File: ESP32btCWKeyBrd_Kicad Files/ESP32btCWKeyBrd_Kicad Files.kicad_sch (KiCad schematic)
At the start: 20 parts, among them J1 CW Key Out, J2 3.5" TFT ILI9488, J3 Audio In Jack, J4 Conn_01x02_MountingPin, Q1 MMBT3904, Q2 MMBT3906, Q3 D4184, U1 ESP32-DEVKIT-V1

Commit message: Incremental Commit
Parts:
- added SW1: SW_Push_SPDT, symbol Switch:SW_Push_SPDT
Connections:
- net +5V: now also SW1.3 (C); no longer J4.1 (Pin_1)
- new net: J4.1 (Pin_1), SW1.2 (B)
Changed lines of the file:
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@@
+    (stroke (width 0) (type default))
+  )
+  (wire (pts (xy 130.81 38.1) (xy 140.97 38.1))
     (stroke (width 0) (type default))
   )
@@
         (path "/3f3f0b47-94ce-4e4b-9adc-e767077ae590"
           (reference "Q2") (unit 1)
+        )
+      )
+    )
+  )
+  (symbol (lib_id "Switch:SW_Push_SPDT") (at 125.73 38.1 0) (mirror y) (unit 1)
+    (in_bom yes) (on_board yes) (dnp no) (fields_autoplaced)
+    (property "Reference" "SW1" (at 125.73 30.48 0)
+      (effects (font (size 1.27 1.27)))
+    )
+    (property "Value" "SW_Push_SPDT" (at 125.73 33.02 0)
+      (effects (font (size 1.27 1.27)))
+    )
+    (property "Footprint" "" (at 125.73 38.1 0)
+      (effects (font (size 1.27 1.27)) hide)
+    )
+    (property "Datasheet" "~" (at 125.73 38.1 0)
+      (effects (font (size 1.27 1.27)) hide)
+    )
+    (pin "3")
+    (pin "1")
+    (pin "2")
+    (instances
+      (project "ESP32btCWKeyBrd_Kicad Files"
+        (path "/3f3f0b47-94ce-4e4b-9adc-e767077ae590"
+          (reference "SW1") (unit 1)
         )
       )
@@
     )
   )
-  (symbol (lib_id "power:+5V") (at 140.97 38.1 90) (unit 1)
-    (in_bom yes) (on_board yes) (dnp no) (fields_autoplaced)
-    (property "Reference" "#PWR015" (at 144.78 38.1 0)
-      (effects (font (size 1.27 1.27)) hide)
-    )
-    (property "Value" "+5V" (at 137.16 38.1 90)
-      (effects (font (size 1.27 1.27)) (justify left))
-    )
-    (property "Footprint" "" (at 140.97 38.1 0)
-      (effects (font (size 1.27 1.27)) hide)
-    )
-    (property "Datasheet" "" (at 140.97 38.1 0)
-      (effects (font (size 1.27 1.27)) hide)
-    )
+  (symbol (lib_id "power:+5V") (at 120.65 40.64 90) (unit 1)
+    (in_bom yes) (on_board yes) (dnp no) (fields_autoplaced)
+    (property "Reference" "#PWR015" (at 124.46 40.64 0)
+      (effects (font (size 1.27 1.27)) hide)
+    )
+    (property "Value" "+5V" (at 116.84 40.64 90)
+      (effects (font (size 1.27 1.27)) (justify left))
+    )
+    (property "Footprint" "" (at 120.65 40.64 0)
+      (effects (font (size 1.27 1.27)) hide)
+    )
+    (property "Datasheet" "" (at 120.65 40.64 0)
+      (effects (font (size 1.27 1.27)) hide)
+    )

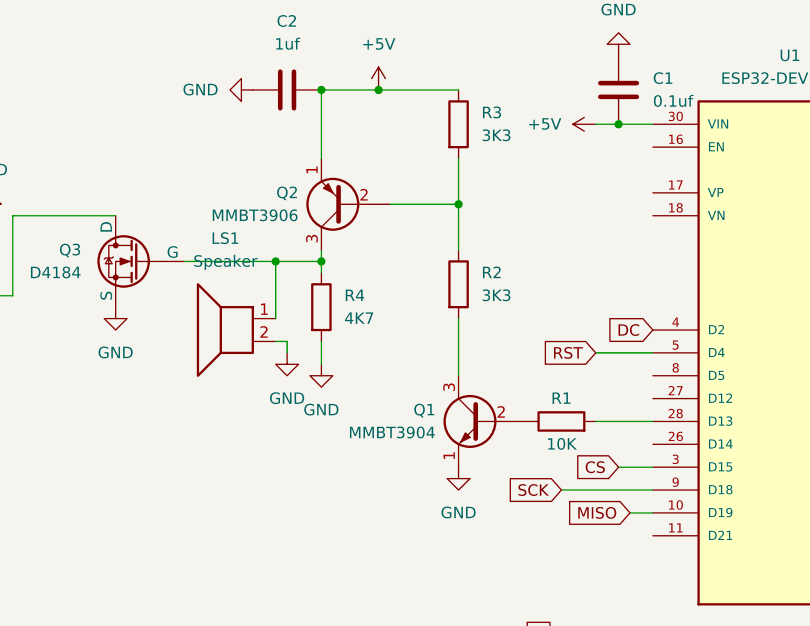
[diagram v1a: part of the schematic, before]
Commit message: Fixed the PCB
Unfortunately after I ordered the original set :(
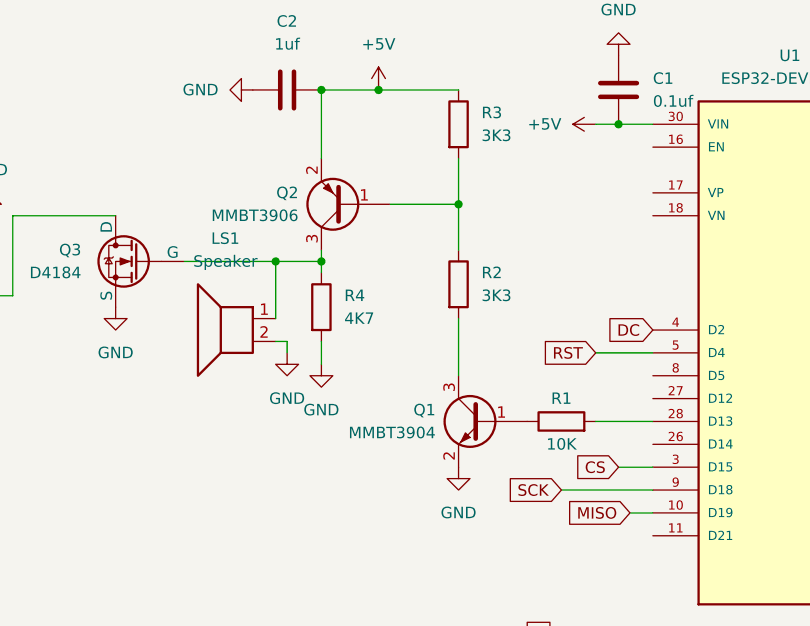
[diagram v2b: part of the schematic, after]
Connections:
- net +5V: now also Q2.2 (E); no longer Q2.1 (E)
- net GND: now also Q1.2 (E); no longer Q1.1 (E)
- net at R2.1, R3.2: now also Q2.1 (B); no longer Q2.2 (B)
- net at R1.1: now also Q1.1 (B); no longer Q1.2 (B)

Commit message: Updates on drawings
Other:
- title: (none) -> ESP32 Bluetooth Keyboard CW Keyer
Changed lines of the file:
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@@
 (kicad_sch (version 20230121) (generator eeschema)
   (paper "A4")
+  (title_block
+    (title "ESP32 Bluetooth Keyboard CW Keyer")
+    (date "2024-12-27")
+    (rev "2")
+    (comment 1 "SMD PCD by atoughram")
+    (comment 2 "Forked from jmharvey1")
+  )
   (junction (at 205.74 74.93) (diameter 0) (color 0 0 0 0)
   )
